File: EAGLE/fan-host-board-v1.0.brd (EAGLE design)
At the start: 45.7 x 25.4 mm, 37 parts

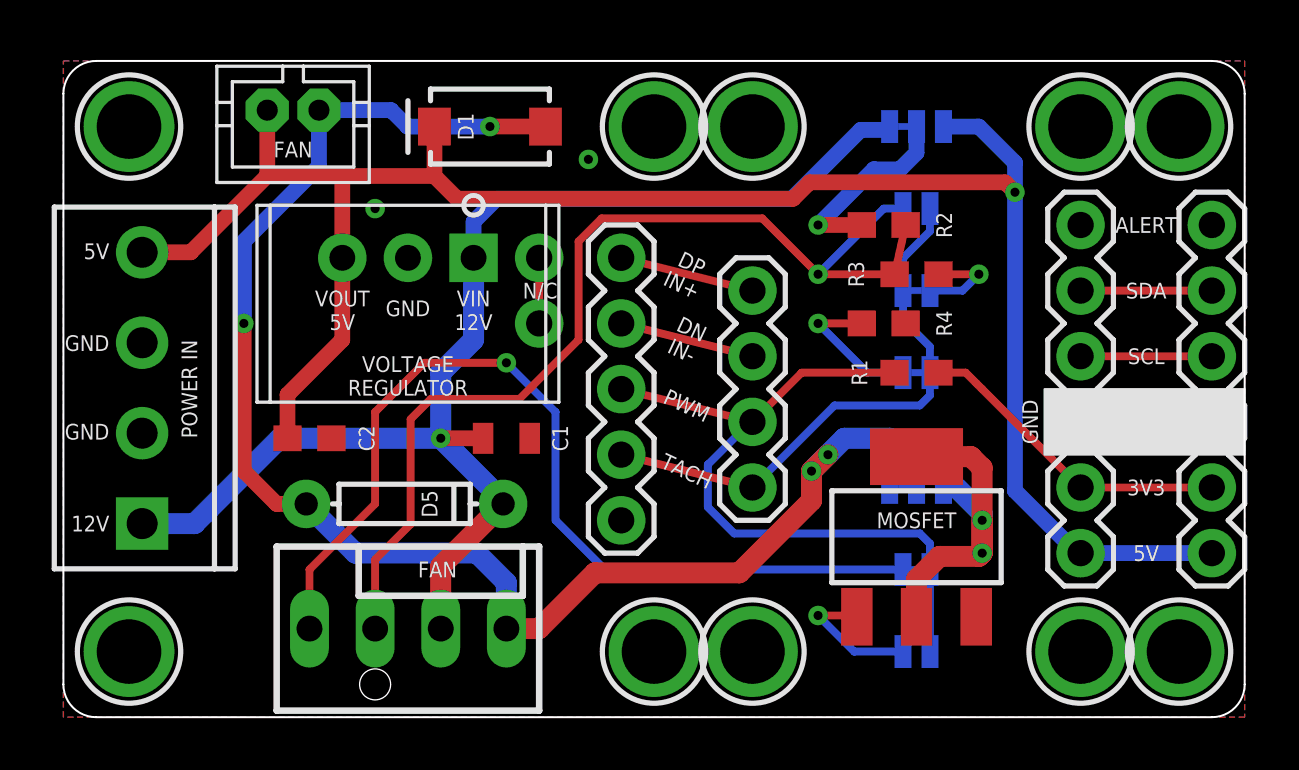
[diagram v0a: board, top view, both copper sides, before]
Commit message: added active buzzer
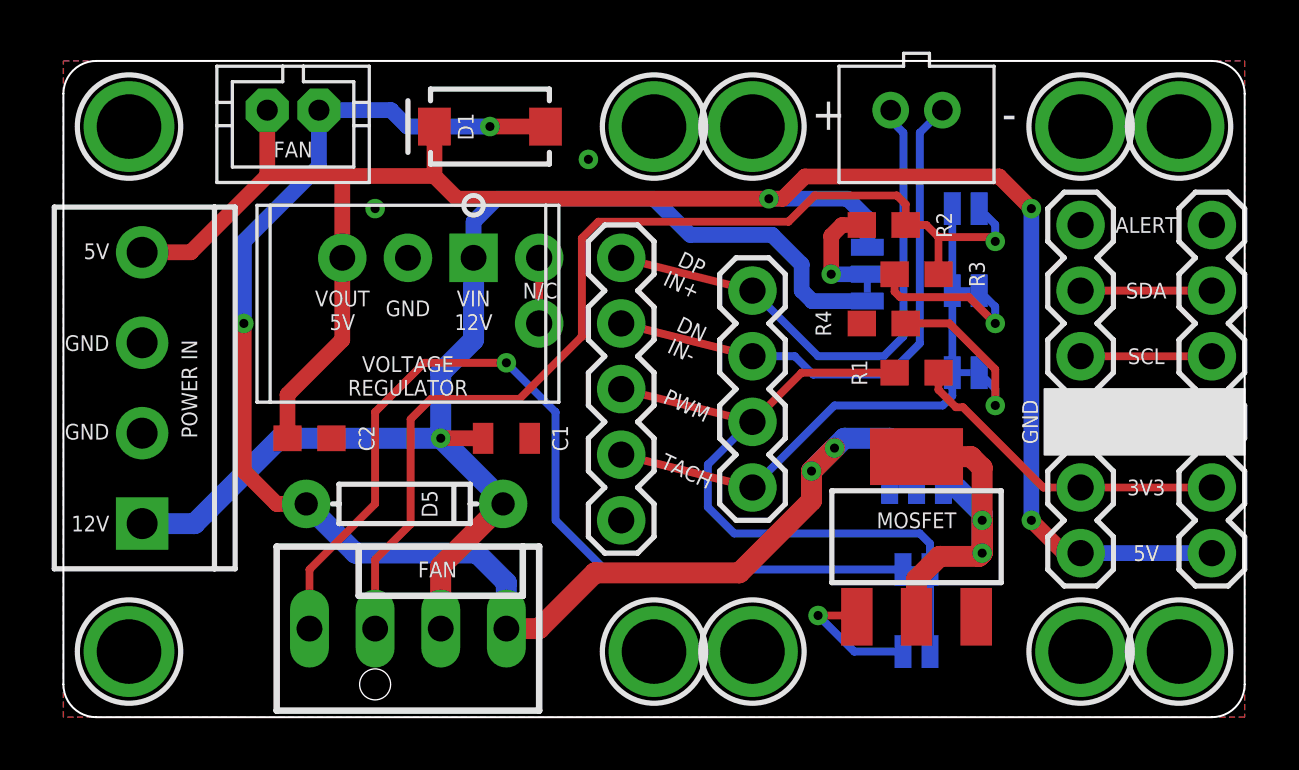
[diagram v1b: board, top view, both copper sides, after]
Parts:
- added CN1: (no value), adafruit:JST-PH-2-THM
- moved JP1 6.02 mm to (31.1, 17.1), turned to 270 degrees
- moved JP2 1.90 mm to (34.9, 19.7), turned to 180 degrees
- moved JP3 1.90 mm to (34.9, 16.5)
- moved JP4 1.90 mm to (34.9, 13.3), turned to 180 degrees
- turned R3 to 180 degrees
- turned R4 to 180 degrees
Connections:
- net IN+: now also CN1.1
- net IN-: now also CN1.2
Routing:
- net IN-: track 5.24 -> 21.9 mm
- net IN+: track 5.24 -> 21.4 mm
- net N$4: track 7.67 -> 4.24 mm
- net N$5: track 3.72 -> 6.61 mm
- net 5V: track 75.9 -> 77.3 mm, vias 1 -> 3
- net N$6: track 5.77 -> 7.13 mm
- net TACH/SENS: track 40.0 -> 41.3 mm
